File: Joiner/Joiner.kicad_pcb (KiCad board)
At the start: 4 copper layers, 32 x 59 mm, 26 parts, among them J1 Conn_02x04_Odd_Even, J2 Conn_02x04_Odd_Even, J3 AudioJack2_Ground, U1 OPA1656

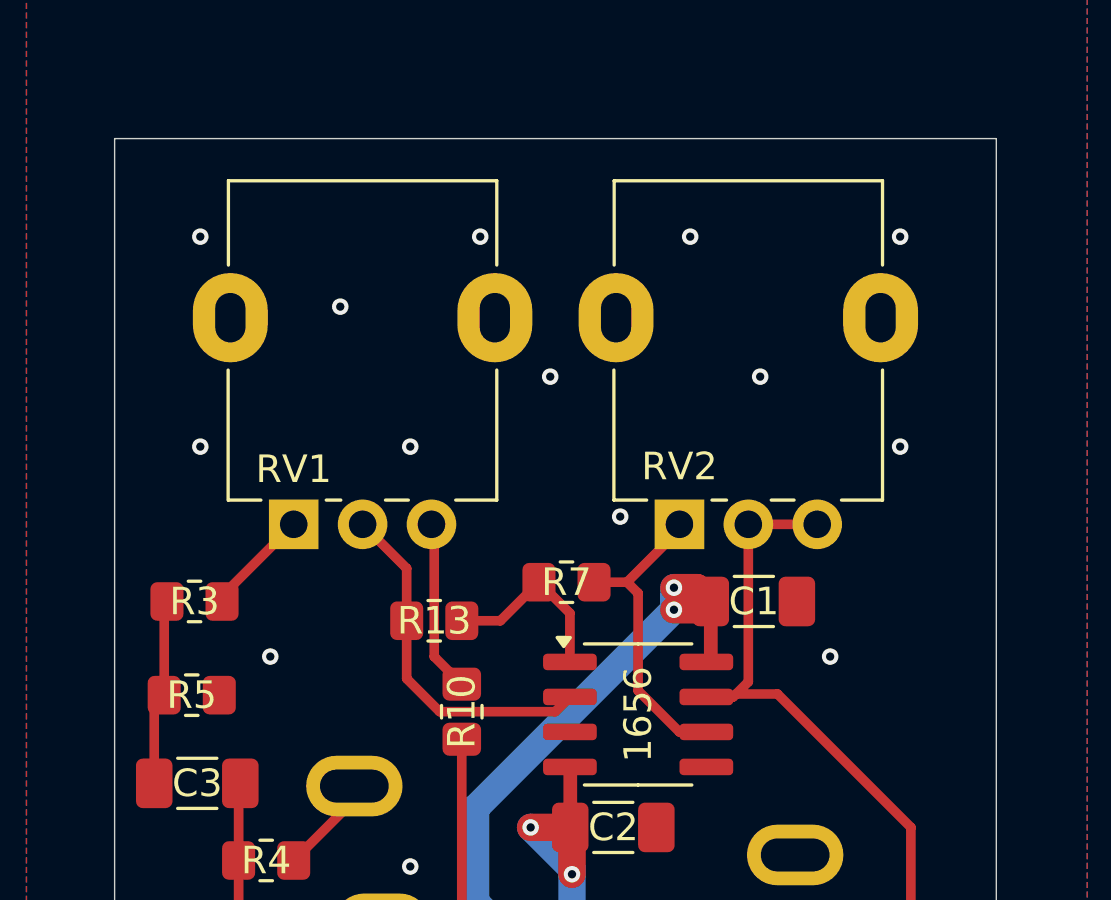
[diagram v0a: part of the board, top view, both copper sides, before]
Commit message: Add tentative drill patterns for Tayda enclosure drilling
Fix up the layout so that the same drill pattern with three holes for
pots/switches works for both the Baxandall and Boost, and move some of
the other controls around to make for whole numbers in mm.

Do the drill patterns work? They match the PCB layout, but let's see
about the vertical sides...  Tayda drilling is running behind, so I
don't think I'll see the actual result for a couple of weeks.

Also fix some typos in the readme while updating it about the drill
patterns.

Signed-off-by: Linus Torvalds <torvalds@linux-foundation.org>
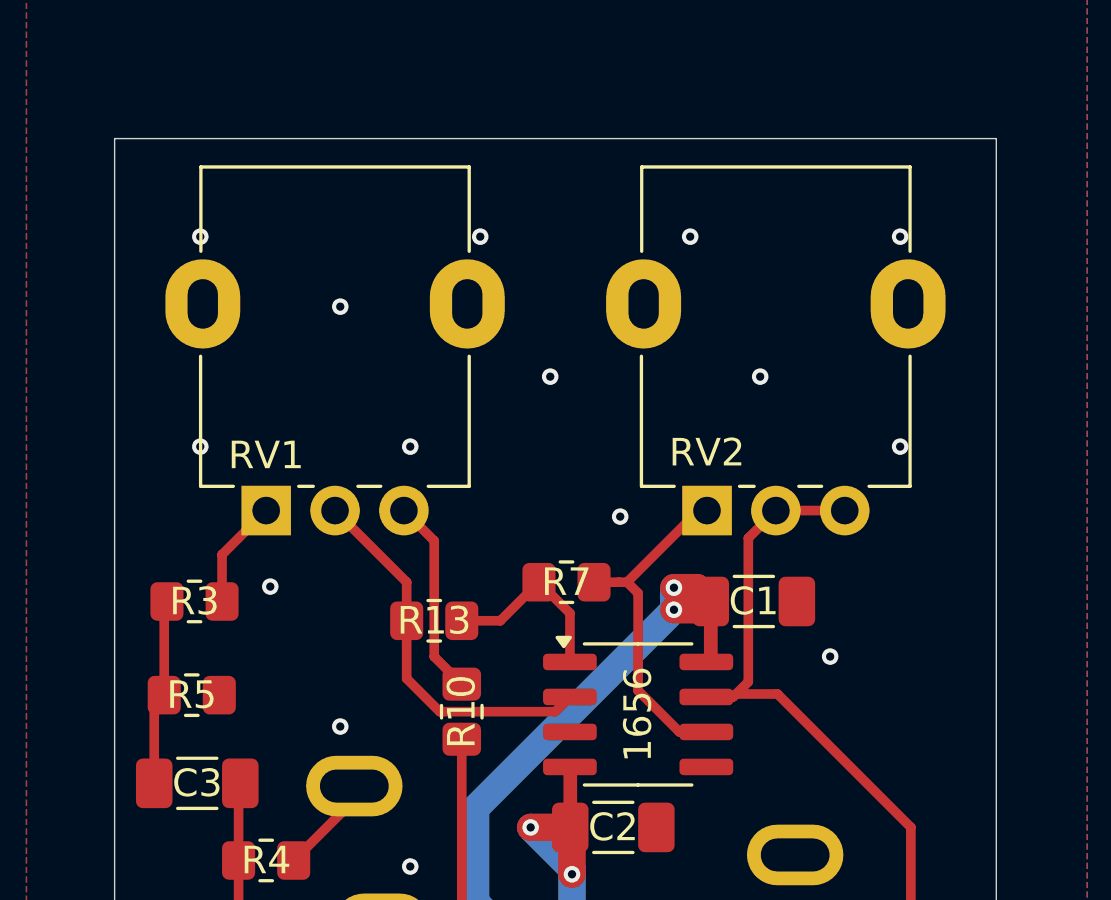
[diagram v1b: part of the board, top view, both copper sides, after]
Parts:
- moved RV1 1.12 mm to (189.5, 77.5)
- moved RV2 1.12 mm to (205.5, 77.5)
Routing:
- net Net-(U1B--): track 11.3 -> 12.4 mm
- net Net-(U1B-OUT): track 45.6 -> 46.5 mm
- net Net-(U1A--): track 12.9 -> 13.8 mm
- net Net-(R10-Pad2): track 6.26 -> 7.17 mm
- net GND: vias 34 -> 35
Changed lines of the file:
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@@
 	(footprint "Potentiometer_THT:Potentiometer_Alpha_RD901F-40-00D_Single_Vertical"
 		(layer "F.Cu")
-		(at 190.5 78 90)
+		(at 189.5 77.5 90)
 		(descr "Potentiometer, vertical, 9mm, single, http://www.taiwanalpha.com.tw/downloads?target=products&id=113")
 		(tags "potentiometer vertical 9mm single")
@@
 	(footprint "Potentiometer_THT:Potentiometer_Alpha_RD901F-40-00D_Single_Vertical"
 		(layer "F.Cu")
-		(at 204.5 78 90)
+		(at 205.5 77.5 90)
 		(descr "Potentiometer, vertical, 9mm, single, http://www.taiwanalpha.com.tw/downloads?target=products&id=113")
 		(tags "potentiometer vertical 9mm single")
@@
 	)
 	(via
-		(at 197.27 67.5595)
+		(at 204.89 92.9595)
 		(size 0.6)
 		(drill 0.3)
@@
 	)
 	(via
-		(at 187.11 105.6595)
+		(at 202.35 120.8995)
 		(size 0.6)
 		(drill 0.3)
@@
 	)
 	(via
-		(at 202.35 120.8995)
+		(at 187.11 105.6595)
 		(size 0.6)
 		(drill 0.3)
@@
 	)
 	(via
-		(at 194.73 105.6595)
+		(at 192.19 85.3395)
 		(size 0.6)
 		(drill 0.3)
@@
 	)
 	(via
-		(at 209.97 82.7995)
+		(at 209.97 98.0395)
 		(size 0.6)
 		(drill 0.3)
@@
 	)
 	(via
-		(at 199.81 100.5795)
+		(at 212.51 67.5595)
 		(size 0.6)
 		(drill 0.3)
@@
 	)
 	(via
-		(at 194.73 90.4195)
+		(at 207.43 115.8195)
 		(size 0.6)
 		(drill 0.3)
@@
 	)
 	(via
-		(at 207.43 115.8195)
+		(at 189.65 80.2595)
 		(size 0.6)
 		(drill 0.3)
@@
 	)
 	(via
-		(at 194.73 120.8995)
+		(at 207.43 72.6395)
 		(size 0.6)
 		(drill 0.3)
@@
 	)
 	(via
-		(at 187.11 67.5595)
+		(at 194.73 90.4195)
 		(size 0.6)
 		(drill 0.3)
@@
 	)
 	(via
-		(at 187.11 95.4995)
+		(at 209.97 82.7995)
 		(size 0.6)
 		(drill 0.3)
@@
 	)
 	(via
-		(at 189.65 100.5795)
+		(at 194.73 120.8995)
 		(size 0.6)
 		(drill 0.3)
@@
 	)
 	(via
-		(at 194.73 113.2795)
+		(at 187.11 67.5595)
 		(size 0.6)
 		(drill 0.3)
@@
 	)
 	(via
-		(at 204.89 110.7395)
+		(at 194.73 75.1795)
 		(size 0.6)
 		(drill 0.3)
@@
 	)
 	(via
-		(at 192.19 70.0995)
+		(at 209.97 108.1995)
 		(size 0.6)
 		(drill 0.3)
@@
 	)
 	(via
-		(at 207.43 72.6395)
+		(at 199.81 72.6395)
 		(size 0.6)
 		(drill 0.3)
@@
 	)
 	(via
-		(at 194.73 98.0395)
+		(at 199.81 100.5795)
 		(size 0.6)
 		(drill 0.3)
@@
 	)
 	(via
-		(at 189.65 82.7995)
+		(at 197.27 67.5595)
 		(size 0.6)
 		(drill 0.3)
@@
 	)
 	(via
-		(at 194.73 75.1795)
+		(at 209.97 120.8995)
 		(size 0.6)
 		(drill 0.3)
@@
 	)
 	(via
-		(at 209.97 120.8995)
+		(at 199.81 115.8195)
 		(size 0.6)
 		(drill 0.3)
@@
 	)
 	(via
-		(at 212.51 113.2795)
+		(at 187.11 95.4995)
 		(size 0.6)
 		(drill 0.3)
@@
 	)
 	(via
-		(at 199.81 115.8195)
+		(at 194.73 113.2795)
 		(size 0.6)
 		(drill 0.3)
@@
 	)
 	(via
-		(at 199.81 72.6395)
+		(at 194.73 98.0395)
 		(size 0.6)
 		(drill 0.3)
@@
 	)
 	(via
-		(at 209.97 108.1995)
+		(at 204.89 110.7395)
 		(size 0.6)
 		(drill 0.3)
@@
 	)
 	(via
-		(at 212.51 67.5595)
+		(at 202.35 77.7195)
 		(size 0.6)
 		(drill 0.3)
@@
 	)
 	(via
-		(at 204.89 67.5595)
+		(at 187.11 75.1795)
 		(size 0.6)
 		(drill 0.3)
@@
 	)
 	(via
-		(at 202.35 77.7195)
+		(at 194.73 105.6595)
 		(size 0.6)
 		(drill 0.3)
@@
 	)
 	(via
-		(at 204.89 92.9595)
+		(at 212.51 113.2795)
 		(size 0.6)
 		(drill 0.3)
@@
 	)
 	(via
-		(at 209.97 98.0395)
+		(at 192.19 70.0995)
 		(size 0.6)
 		(drill 0.3)
@@
 	)
 	(via
-		(at 187.11 75.1795)
+		(at 204.89 67.5595)
+		(size 0.6)
+		(drill 0.3)
+		(layers "F.Cu" "B.Cu")
+		(free yes)
+		(net 1)
+	)
+	(via
+		(at 189.65 100.5795)
 		(size 0.6)
 		(drill 0.3)
@@
 	)
 	(segment
-		(start 201.8625 111.7)
-		(end 206.8 106.7625)
+		(start 207 83.714999)
+		(end 206.5575 84.1575)
 		(width 0.35)
 		(layer "F.Cu")
@@
 	)
 	(segment
-		(start 206.8 106.7625)
-		(end 206.8 98)
+		(start 208 77.5)
+		(end 207 78.5)
 		(width 0.35)
 		(layer "F.Cu")
@@
 	)
 	(segment
-		(start 206.5575 84.1575)
-		(end 207 83.714999)
+		(start 201.8625 111.7)
+		(end 206.8 106.7625)
+		(width 0.35)
+		(layer "F.Cu")
+		(net 7)
+	)
+	(segment
+		(start 206.8 106.7625)
+		(end 206.8 98)
 		(width 0.35)
 		(layer "F.Cu")
@@
 	)
 	(segment
-		(start 207 83.714999)
-		(end 207 78)
+		(start 207 78.5)
+		(end 207 83.714999)
+		(width 0.35)
+		(layer "F.Cu")
+		(net 7)
+	)
+	(segment
+		(start 210.5 77.5)
+		(end 208 77.5)
 		(width 0.35)
 		(layer "F.Cu")
@@
 	)
 	(segment
-		(start 207 78)
-		(end 209.5 78)
-		(width 0.35)
-		(layer "F.Cu")
-		(net 7)
-	)
-	(segment
 		(start 206.8 98)
 		(end 212.9 91.9)
@@
 	)
 	(segment
-		(start 187.9 80.8)
-		(end 187.9 80.6)
+		(start 187.9 79.1)
+		(end 189.5 77.5)
 		(width 0.35)
 		(layer "F.Cu")
@@
 	)
 	(segment
-		(start 187.9 80.6)
-		(end 190.5 78)
+		(start 187.9 80.8)
+		(end 187.9 79.1)
 		(width 0.35)
 		(layer "F.Cu")
@@
 	(segment
 		(start 202.6 80.1)
-		(end 201.4 80.1)
+		(end 202.3 80.1)
 		(width 0.35)
 		(layer "F.Cu")
@@
 	)
 	(segment
-		(start 204.5 78.2)
-		(end 204.5 78)
+		(start 205.2 77.5)
+		(end 202.6 80.1)
 		(width 0.35)
 		(layer "F.Cu")
@@
 	)
 	(segment
-		(start 202.6 80.1)
-		(end 204.5 78.2)
+		(start 205.5 77.5)
+		(end 205.2 77.5)
+		(width 0.35)
+		(layer "F.Cu")
+		(net 18)
+	)
+	(segment
+		(start 202.3 80.1)
+		(end 201.4 80.1)
 		(width 0.35)
 		(layer "F.Cu")
@@
 	)
 	(segment
-		(start 195.6 82.8)
-		(end 195.6 78.1)
+		(start 196.6 83.8)
+		(end 195.6 82.8)
 		(width 0.35)
 		(layer "F.Cu")
@@
 	)
 	(segment
-		(start 196.6 83.8)
-		(end 195.6 82.8)
+		(start 195.6 82.8)
+		(end 195.6 78.6)
 		(width 0.35)
 		(layer "F.Cu")
@@
 	)
 	(segment
-		(start 195.6 78.1)
-		(end 195.5 78)
+		(start 195.6 78.6)
+		(end 194.5 77.5)
 		(width 0.35)
 		(layer "F.Cu")
@@
 	)
 	(segment
-		(start 194.6 79.6)
-		(end 193 78)
+		(start 194.6 80.1)
+		(end 192 77.5)
 		(width 0.35)
 		(layer "F.Cu")
@@
 	)
 	(segment
-		(start 194.6 81.5)
-		(end 194.6 79.6)
+		(start 195.8 84.8)
+		(end 194.6 83.6)
 		(width 0.35)
 		(layer "F.Cu")
@@
 	)
 	(segment
-		(start 195.8 84.8)
-		(end 194.6 83.6)
+		(start 194.6 81.5)
+		(end 194.6 80.1)
 		(width 0.35)
 		(layer "F.Cu")
@@
 	)
 	(group "ViaStitching GND"
-		(members "0c0cd2a5-f026-4b3c-b0cf-6c279c548c6b" "12e55c6c-7714-4460-b64e-213bb6ce65da"
-			"2ebba02c-f40a-4432-a4b5-64c52e5c4e39" "2f2a05e7-af5e-4f48-a181-4738eb76d796"
-			"3144e78d-8c97-4334-b6f9-8ad87b3c4372" "31566227-c51a-430d-ae42-2886de8b5cdd"
-			"316b4af8-e7b9-4a82-a3cc-f6a93173b8e4" "4164ed80-933b-4aaa-91a3-c7c2a6dd7733"
-			"4308da09-f4c9-4b36-b5ac-7789e0c7455b" "53f87aac-32fe-4692-87c2-47de8566db46"
-			"5d70bc06-ee0a-4548-9663-99fb24ac684f" "644a3186-74fe-49a3-9f26-09856a07492d"
-			"692ae190-41d6-427f-9935-4c82984e2461" "6e744301-43fa-466b-aeeb-365da1250c74"
-			"6f7bbb8e-61ee-462a-b697-5fdf36824108" "716895de-88ae-4372-b205-aa3ee5b67fe6"
-			"7892dd85-a0d5-4000-9b58-adf4f45dbbce" "9821463a-337b-432b-adbf-7b9dc7a3302e"
-			"ac5c631f-3c99-4fa0-8755-3559530638f9" "b993dc95-dc50-4064-bf78-3fc5f848e246"
-			"bd4c6104-ab7a-4953-8525-fc84cf536889" "bdd3ee04-4fa3-406d-b751-077961e98b51"
-			"c1aed2cd-0415-4350-af87-bd3e1de8ba3e" "cd4f63ed-e588-4ac7-a87f-0a312ef92510"
-			"d0989f9f-1f9f-4c5d-8a30-eeb18c6aa7c9" "da20daa7-c71c-4990-b5bc-ec074614d796"
-			"da5febde-cacd-4af7-bb25-d4b649f2fa30" "dba422ac-2815-40e1-9be6-600eb69c0dfd"
-			"e05dad04-42fb-4533-baae-60748d2c49f4" "f2b85952-556b-452f-93cd-3b20adcafb2e"
-			"f5af6623-d134-405d-98f2-2674be8fecd4" "fb2c6dbf-d465-4d0a-8860-5d2c45d58ce7"
-			"fbc8b5a0-9231-4bc5-922a-ac10101180f9"
+		(members "0a96b8e6-beb1-4f31-81e7-7c032a62bc46" "0aa19400-7948-4be8-b766-01f625c9b7cf"
+			"0eb7db5b-2b98-4093-b421-1459afa47473" "27e45abd-6f8e-46a4-8351-b97b7c0b1685"
+			"349b41f3-351a-4b3e-801e-ee1d23adac37" "34fa91c9-a3c0-4428-8f90-d33d718991e5"
+			"34fdfb69-ee4a-40d5-a7a8-8d0cc3211acf" "384c0419-1c8d-4451-9c77-4a32e77776db"
+			"42469686-3e27-437f-a131-0925c96ed15c" "5412bd5d-c7c3-46da-8339-965d4e136334"
+			"5b337829-8c8d-44b2-a277-c754539ecca0" "5c10d4f9-c86f-4afd-9f36-f86fbe07cff0"
+			"6454bb6b-04f1-4dd7-b99d-1f1295caa04b" "65498aa3-7eba-4647-9b69-8f3dd6910cd8"
+			"744fc323-564d-4058-8d72-a64a096ee78d" "755e5338-5ca3-4b66-96f0-94e0175eb622"
+			"79db073a-8730-4b3f-b23c-3adba1a0462c" "7a4d5610-5e9d-4ed4-b27e-9801c955437c"
+			"a7028bb0-4de9-41df-9be4-4142ff709205" "ad99c56a-692b-4389-8f0d-2cb191589ef0"
+			"b227e3ef-f180-42b5-8d04-05ac18ce7de0" "b2f082f2-dac7-4c44-9dd7-4e77259b4461"
+			"b37e0728-3fe4-421b-b195-4e9f920184ae" "ba5c1138-303c-4739-9e5b-67d77225f1de"
+			"bb1d2dfc-55dc-46be-94df-6b01c6538183" "bee80c4b-8c08-4b84-b592-5f222375d94d"
+			"c4ad70a3-89b1-4523-a4f5-ee2e4664eb99" "cec1ccd0-03f2-4f43-aea4-f8ce45a7ba3b"
+			"d2db52d9-5dcf-497e-bfd4-594f167ceb93" "d4fd5606-0043-4980-82de-e022dd6c1b5b"
+			"dbb588a5-2e10-43ac-af88-074f3be8d991" "dc4564ed-a1ee-4821-83b2-70b07cef12c4"
+			"df9643e2-2607-4d66-aec3-5a3ed5a6733e" "e7c45b23-4b99-457a-8248-008094e907ea"
 		)
 	)
